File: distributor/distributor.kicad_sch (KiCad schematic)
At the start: 34 parts, among them J1 Cerebellum, J10 CAN FD, J11 CAN FD, J12 CAN FD, J13 CAN FD, J14 ArmR, J15 CAN FD, J16 ArmL, J2 Cerebrum, J3 PowerIO, J4 Back, J5 LegL, J6 ArmL, J7 LegR, J8 ArmR, J9 PowerIO, U1 TPS54231

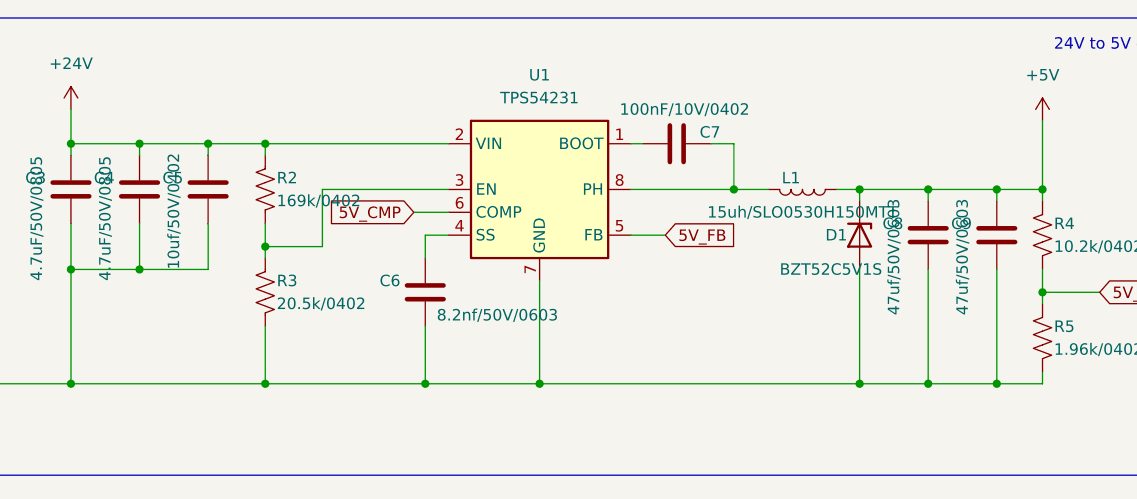
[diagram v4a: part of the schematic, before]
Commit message: [Fix] Correct capacities in 24Vto5V converter
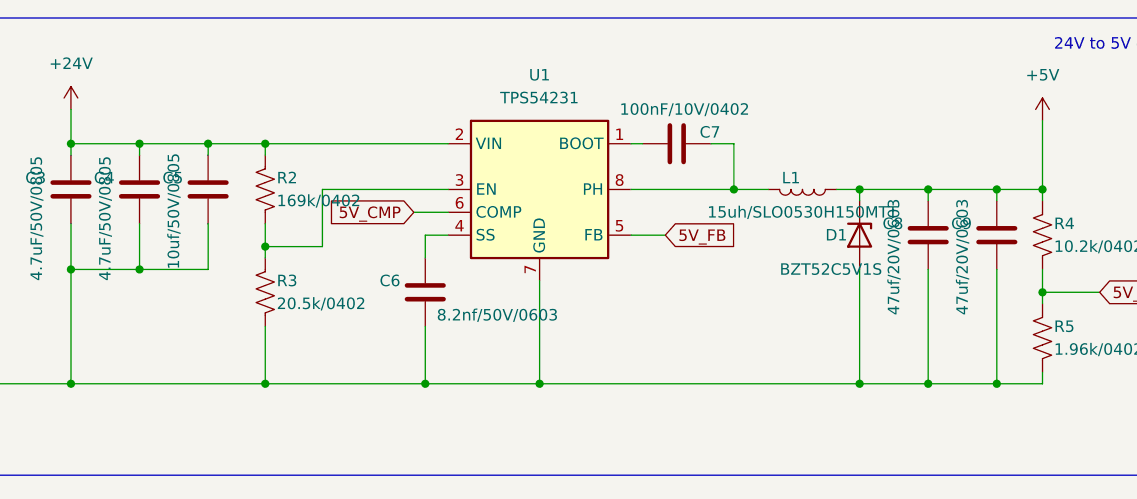
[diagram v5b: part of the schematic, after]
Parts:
- C5: value 10uf/50V/0402 -> 10uf/50V/0805; footprint Capacitor_SMD:C_0402_1005Metric -> Capacitor_SMD:C_0805_2012Metric
- C8, C9: value 47uf/50V/0603 -> 47uf/20V/0603
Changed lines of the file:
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@@
       (effects (font (size 1.27 1.27)) (justify left))
     )
-    (property "Value" "47uf/50V/0603" (id 1) (at 238.76 49.53 90)
+    (property "Value" "47uf/20V/0603" (id 1) (at 238.76 49.53 90)
       (effects (font (size 1.27 1.27)) (justify left))
     )
@@
       (effects (font (size 1.27 1.27)) (justify left))
     )
-    (property "Value" "10uf/50V/0402" (id 1) (at 151.13 44.45 90)
-      (effects (font (size 1.27 1.27)) (justify left))
-    )
-    (property "Footprint" "Capacitor_SMD:C_0402_1005Metric" (id 2) (at 155.9052 39.37 0)
+    (property "Value" "10uf/50V/0805" (id 1) (at 151.13 44.45 90)
+      (effects (font (size 1.27 1.27)) (justify left))
+    )
+    (property "Footprint" "Capacitor_SMD:C_0805_2012Metric" (id 2) (at 155.9052 39.37 0)
       (effects (font (size 1.27 1.27)) hide)
     )
@@
       (effects (font (size 1.27 1.27)) (justify left))
     )
-    (property "Value" "47uf/50V/0603" (id 1) (at 231.14 49.53 90)
+    (property "Value" "47uf/20V/0603" (id 1) (at 231.14 49.53 90)
       (effects (font (size 1.27 1.27)) (justify left))
     )
@@
     )
     (path "/56bc519f-b580-4182-9554-22c972ce4cce"
-      (reference "C5") (unit 1) (value "10uf/50V/0402") (footprint "Capacitor_SMD:C_0402_1005Metric")
+      (reference "C5") (unit 1) (value "10uf/50V/0805") (footprint "Capacitor_SMD:C_0805_2012Metric")
     )
     (path "/d9f7fb4b-1330-4ee6-9cef-3c53b9842086"
@@
     )
     (path "/af8648b1-8b99-4ba3-8f97-37142800fa42"
-      (reference "C8") (unit 1) (value "47uf/50V/0603") (footprint "Capacitor_SMD:C_0603_1608Metric")
+      (reference "C8") (unit 1) (value "47uf/20V/0603") (footprint "Capacitor_SMD:C_0603_1608Metric")
     )
     (path "/2c0acf60-d553-4a25-820b-80d67bdb4748"
-      (reference "C9") (unit 1) (value "47uf/50V/0603") (footprint "Capacitor_SMD:C_0603_1608Metric")
+      (reference "C9") (unit 1) (value "47uf/20V/0603") (footprint "Capacitor_SMD:C_0603_1608Metric")
     )
     (path "/3752aeae-d122-48ec-894e-c6e390c1dccf"

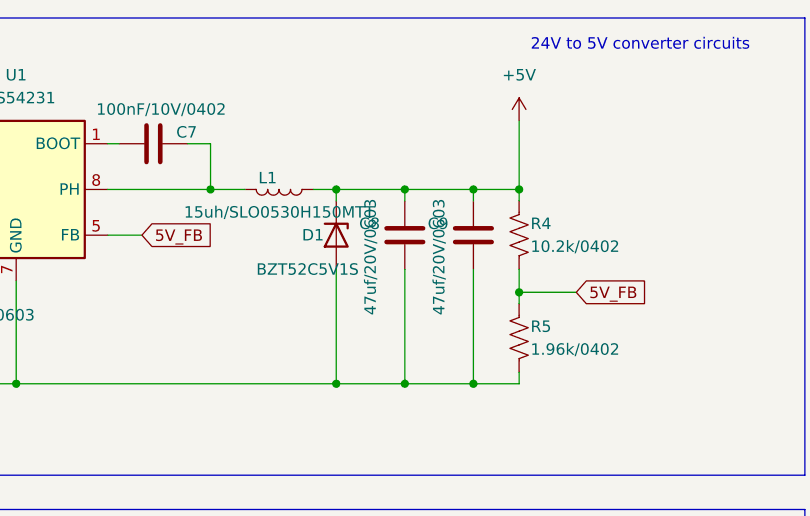
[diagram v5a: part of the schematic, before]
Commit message: [Fix] Correct capacities in 24Vto5V again.
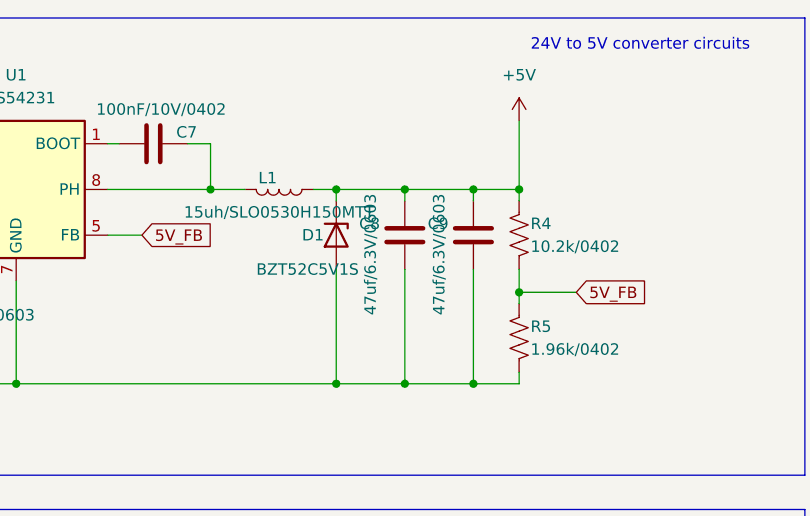
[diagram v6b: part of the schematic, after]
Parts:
- C8, C9: value 47uf/20V/0603 -> 47uf/6.3V/0603
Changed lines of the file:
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@@
       (effects (font (size 1.27 1.27)) (justify left))
     )
-    (property "Value" "47uf/20V/0603" (id 1) (at 238.76 49.53 90)
+    (property "Value" "47uf/6.3V/0603" (id 1) (at 238.76 49.53 90)
       (effects (font (size 1.27 1.27)) (justify left))
     )
@@
       (effects (font (size 1.27 1.27)) (justify left))
     )
-    (property "Value" "47uf/20V/0603" (id 1) (at 231.14 49.53 90)
+    (property "Value" "47uf/6.3V/0603" (id 1) (at 231.14 49.53 90)
       (effects (font (size 1.27 1.27)) (justify left))
     )
@@
     )
     (path "/af8648b1-8b99-4ba3-8f97-37142800fa42"
-      (reference "C8") (unit 1) (value "47uf/20V/0603") (footprint "Capacitor_SMD:C_0603_1608Metric")
+      (reference "C8") (unit 1) (value "47uf/6.3V/0603") (footprint "Capacitor_SMD:C_0603_1608Metric")
     )
     (path "/2c0acf60-d553-4a25-820b-80d67bdb4748"
-      (reference "C9") (unit 1) (value "47uf/20V/0603") (footprint "Capacitor_SMD:C_0603_1608Metric")
+      (reference "C9") (unit 1) (value "47uf/6.3V/0603") (footprint "Capacitor_SMD:C_0603_1608Metric")
     )
     (path "/3752aeae-d122-48ec-894e-c6e390c1dccf"

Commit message: [Fix] Correct distributor layout
Signed-off-by: Homalozoa <nx.tardis@gmail.com>
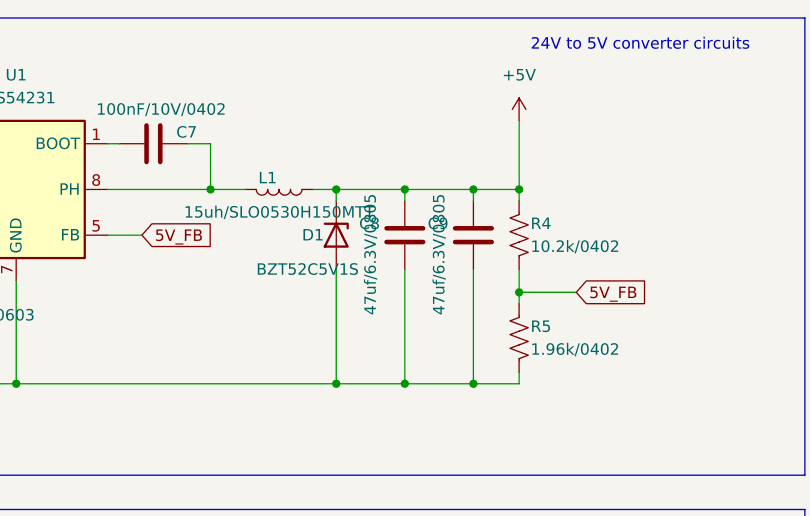
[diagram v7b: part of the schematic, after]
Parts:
- C8, C9: value 47uf/6.3V/0603 -> 47uf/6.3V/0805; footprint Capacitor_SMD:C_0603_1608Metric -> Capacitor_SMD:C_0805_2012Metric
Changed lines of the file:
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@@
       (effects (font (size 1.27 1.27)) (justify left))
     )
-    (property "Value" "47uf/6.3V/0603" (id 1) (at 238.76 49.53 90)
-      (effects (font (size 1.27 1.27)) (justify left))
-    )
-    (property "Footprint" "Capacitor_SMD:C_0603_1608Metric" (id 2) (at 243.5352 44.45 0)
+    (property "Value" "47uf/6.3V/0805" (id 1) (at 238.76 49.53 90)
+      (effects (font (size 1.27 1.27)) (justify left))
+    )
+    (property "Footprint" "Capacitor_SMD:C_0805_2012Metric" (id 2) (at 243.5352 44.45 0)
       (effects (font (size 1.27 1.27)) hide)
     )
@@
       (effects (font (size 1.27 1.27)) (justify left))
     )
-    (property "Value" "47uf/6.3V/0603" (id 1) (at 231.14 49.53 90)
-      (effects (font (size 1.27 1.27)) (justify left))
-    )
-    (property "Footprint" "Capacitor_SMD:C_0603_1608Metric" (id 2) (at 235.9152 44.45 0)
+    (property "Value" "47uf/6.3V/0805" (id 1) (at 231.14 49.53 90)
+      (effects (font (size 1.27 1.27)) (justify left))
+    )
+    (property "Footprint" "Capacitor_SMD:C_0805_2012Metric" (id 2) (at 235.9152 44.45 0)
       (effects (font (size 1.27 1.27)) hide)
     )
@@
     )
     (path "/af8648b1-8b99-4ba3-8f97-37142800fa42"
-      (reference "C8") (unit 1) (value "47uf/6.3V/0603") (footprint "Capacitor_SMD:C_0603_1608Metric")
+      (reference "C8") (unit 1) (value "47uf/6.3V/0805") (footprint "Capacitor_SMD:C_0805_2012Metric")
     )
     (path "/2c0acf60-d553-4a25-820b-80d67bdb4748"
-      (reference "C9") (unit 1) (value "47uf/6.3V/0603") (footprint "Capacitor_SMD:C_0603_1608Metric")
+      (reference "C9") (unit 1) (value "47uf/6.3V/0805") (footprint "Capacitor_SMD:C_0805_2012Metric")
     )
     (path "/3752aeae-d122-48ec-894e-c6e390c1dccf"

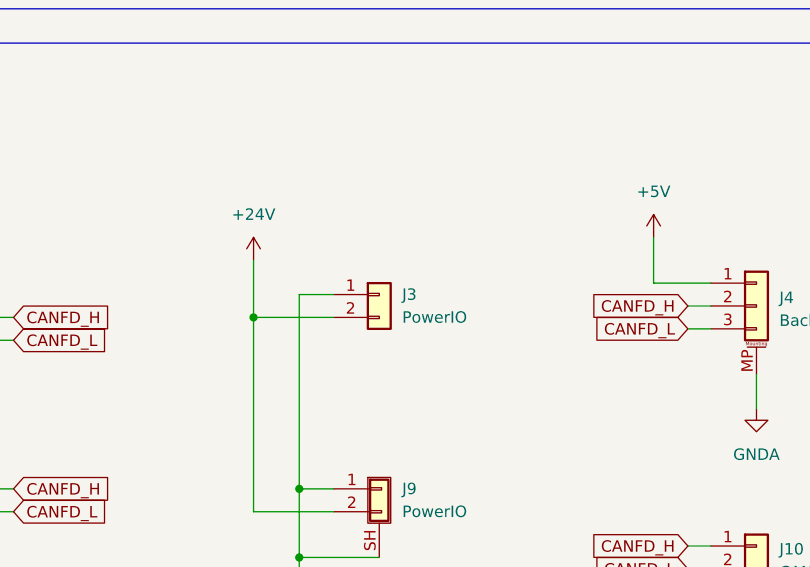
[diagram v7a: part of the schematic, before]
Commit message: [Fix] Connect mounting hole to GNDA
Signed-off-by: Homalozoa <nx.tardis@gmail.com>
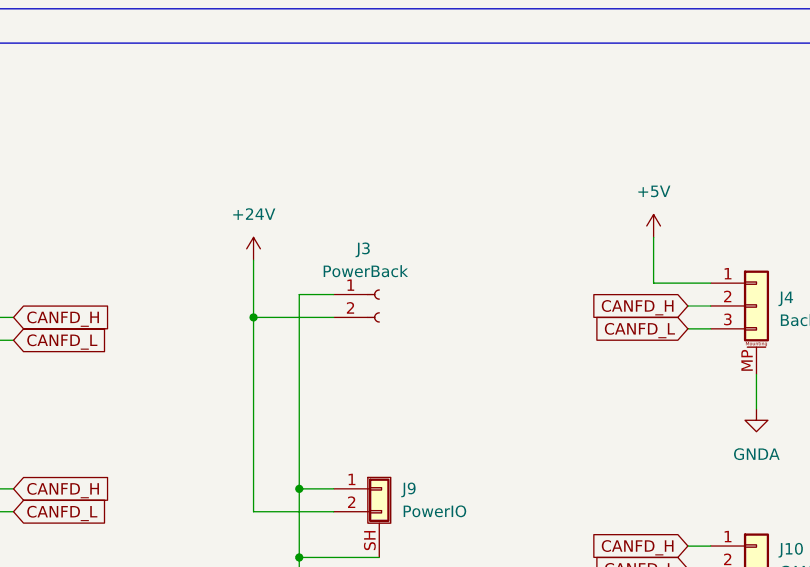
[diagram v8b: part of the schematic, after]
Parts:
- removed J3: PowerIO, Connector_AMASS:AMASS_XT30PW-M_1x02_P2.50mm_Horizontal, symbol Connector_Generic:Conn_01x02
- added J3: PowerBack, Connector_AMASS:AMASS_XT30PW-M_1x02_P2.50mm_Horizontal, symbol Connector:Conn_01x02_Female
- J9: footprint Rolling_Custom:AMASS_XT60PW-M -> Rolling_Custom:AMASS_XT60PW-F
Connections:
- net +24V: now also J3.2 (Pin_2)
- net GNDA: now also J3.1 (Pin_1)
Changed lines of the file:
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@@
+    (pin "2")
+  )
+  (symbol (lib_id "Connector:Conn_01x02_Female") (at 167.64 99.06 0) (unit 1)
+    (in_bom yes) (on_board yes)
+    (property "Reference" "J3" (id 0) (at 165.1 93.98 0)
+      (effects (font (size 1.27 1.27)) (justify left))
+    )
+    (property "Value" "PowerBack" (id 1) (at 161.29 96.52 0)
+      (effects (font (size 1.27 1.27)) (justify left))
+    )
+    (property "Footprint" "Connector_AMASS:AMASS_XT30PW-M_1x02_P2.50mm_Horizontal" (id 2) (at 167.64 99.06 0)
+      (effects (font (size 1.27 1.27)) hide)
+    )
+    (property "Datasheet" "~" (id 3) (at 167.64 99.06 0)
+      (effects (font (size 1.27 1.27)) hide)
+    )
+    (pin "1")
     (pin "2")
   )
@@
       (effects (font (size 1.27 1.27)) (justify left))
     )
-    (property "Footprint" "Rolling_Custom:AMASS_XT60PW-M" (id 2) (at 167.64 120.65 0)
+    (property "Footprint" "Rolling_Custom:AMASS_XT60PW-F" (id 2) (at 167.64 120.65 0)
       (effects (font (size 1.27 1.27)) hide)
     )
@@
     (pin "3")
     (pin "MP")
-  )
-  (symbol (lib_id "Connector_Generic:Conn_01x02") (at 167.64 99.06 0) (unit 1)
-    (in_bom yes) (on_board yes) (fields_autoplaced)
-    (property "Reference" "J3" (id 0) (at 170.18 99.0599 0)
-      (effects (font (size 1.27 1.27)) (justify left))
-    )
-    (property "Value" "PowerIO" (id 1) (at 170.18 101.5999 0)
-      (effects (font (size 1.27 1.27)) (justify left))
-    )
-    (property "Footprint" "Connector_AMASS:AMASS_XT30PW-M_1x02_P2.50mm_Horizontal" (id 2) (at 167.64 99.06 0)
-      (effects (font (size 1.27 1.27)) hide)
-    )
-    (property "Datasheet" "~" (id 3) (at 167.64 99.06 0)
-      (effects (font (size 1.27 1.27)) hide)
-    )
-    (pin "1")
-    (pin "2")
   )
   (symbol (lib_id "power:+5V") (at 198.12 92.71 0) (unit 1)
@@
       (reference "J2") (unit 1) (value "Cerebrum") (footprint "Connector_AMASS:AMASS_XT30PW-M_1x02_P2.50mm_Horizontal")
     )
-    (path "/f172c2a5-8237-40ee-b30c-4d728a071ffd"
-      (reference "J3") (unit 1) (value "PowerIO") (footprint "Connector_AMASS:AMASS_XT30PW-M_1x02_P2.50mm_Horizontal")
+    (path "/87a059b5-72f5-44ba-bdcb-866838421b02"
+      (reference "J3") (unit 1) (value "PowerBack") (footprint "Connector_AMASS:AMASS_XT30PW-M_1x02_P2.50mm_Horizontal")
     )
     (path "/ec5c9fe6-9fdf-4356-99b4-1d2c761f5404"
@@
     )
     (path "/d04c7014-c40a-4aab-8464-ab8a978dba9f"
-      (reference "J9") (unit 1) (value "PowerIO") (footprint "Rolling_Custom:AMASS_XT60PW-M")
+      (reference "J9") (unit 1) (value "PowerIO") (footprint "Rolling_Custom:AMASS_XT60PW-F")
     )
     (path "/556c654f-8d14-4621-b8a9-14c15b80b456"
